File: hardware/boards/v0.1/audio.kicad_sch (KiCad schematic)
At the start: 45 parts, among them J4 SPKR_L, J5 SPKR_R, J8 LINE_OUT, J9 LINE_IN, U24 MIC, U28 TS5A23159RSE, U29 NAU88C22YG, U34 SI4710-B30-GMR, U35 SI4703-C19-GMR, Y3 ASVK-32.768KHZ-LJ-T

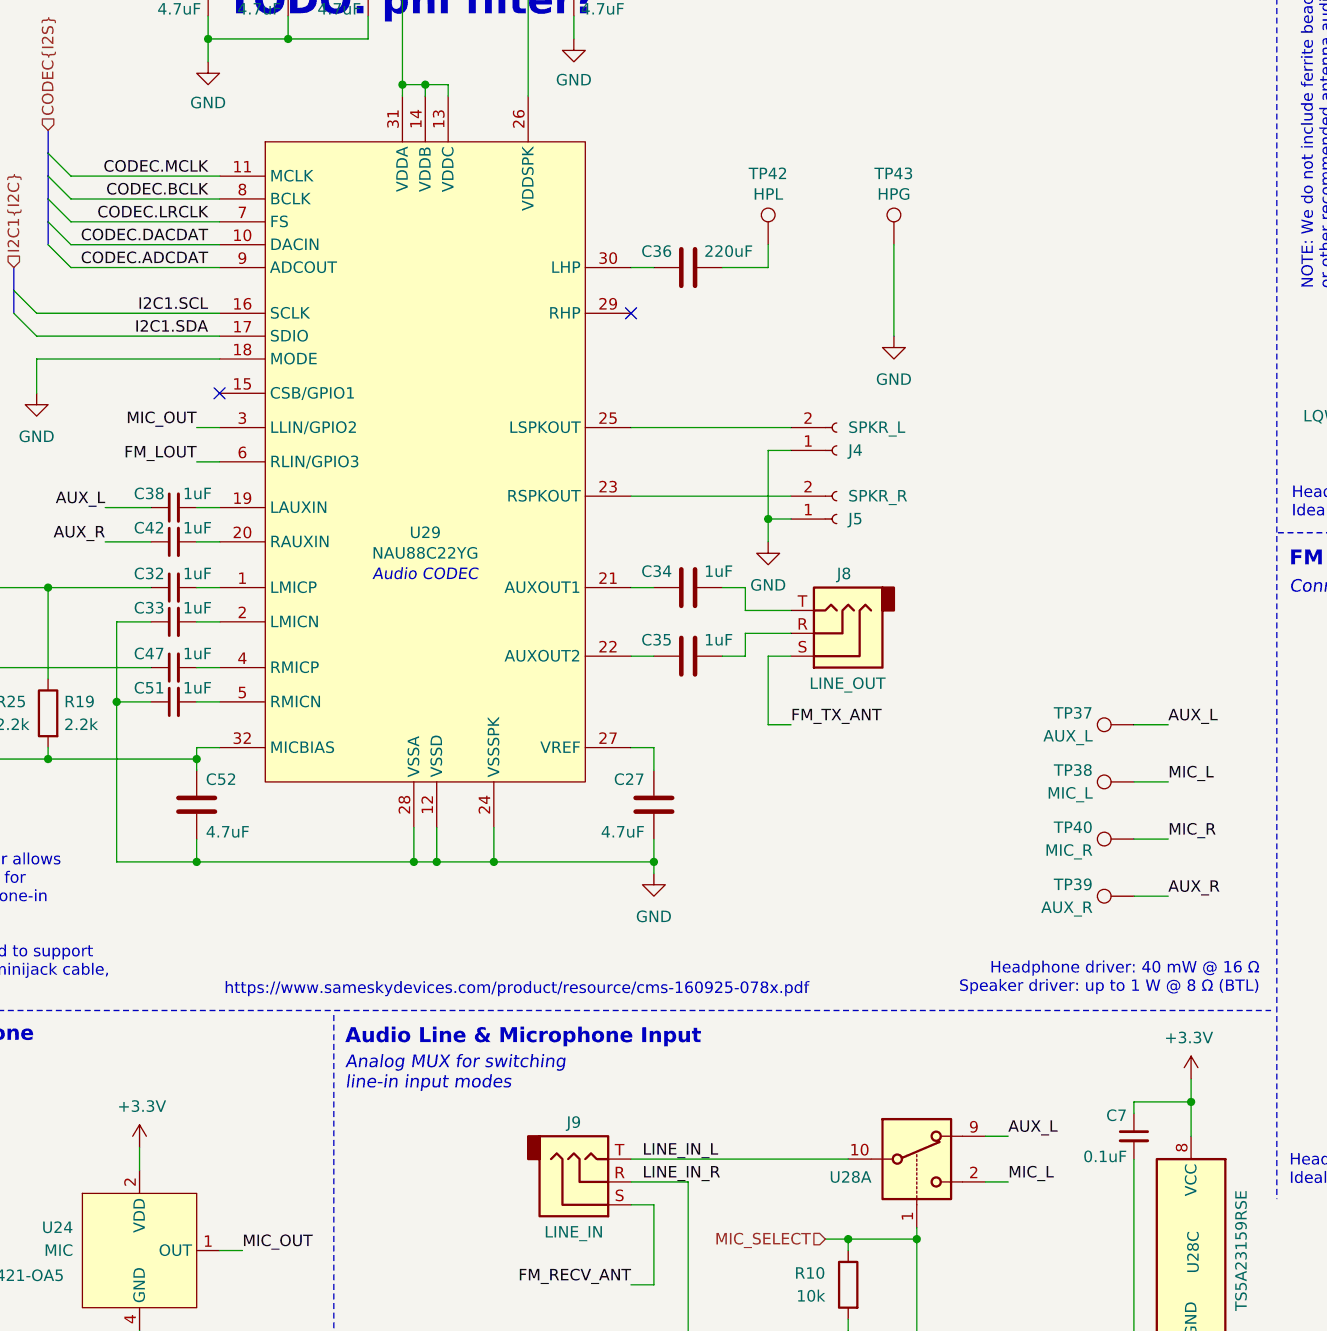
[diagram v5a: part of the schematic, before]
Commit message: feat: routing cleanup and start of BOM selection
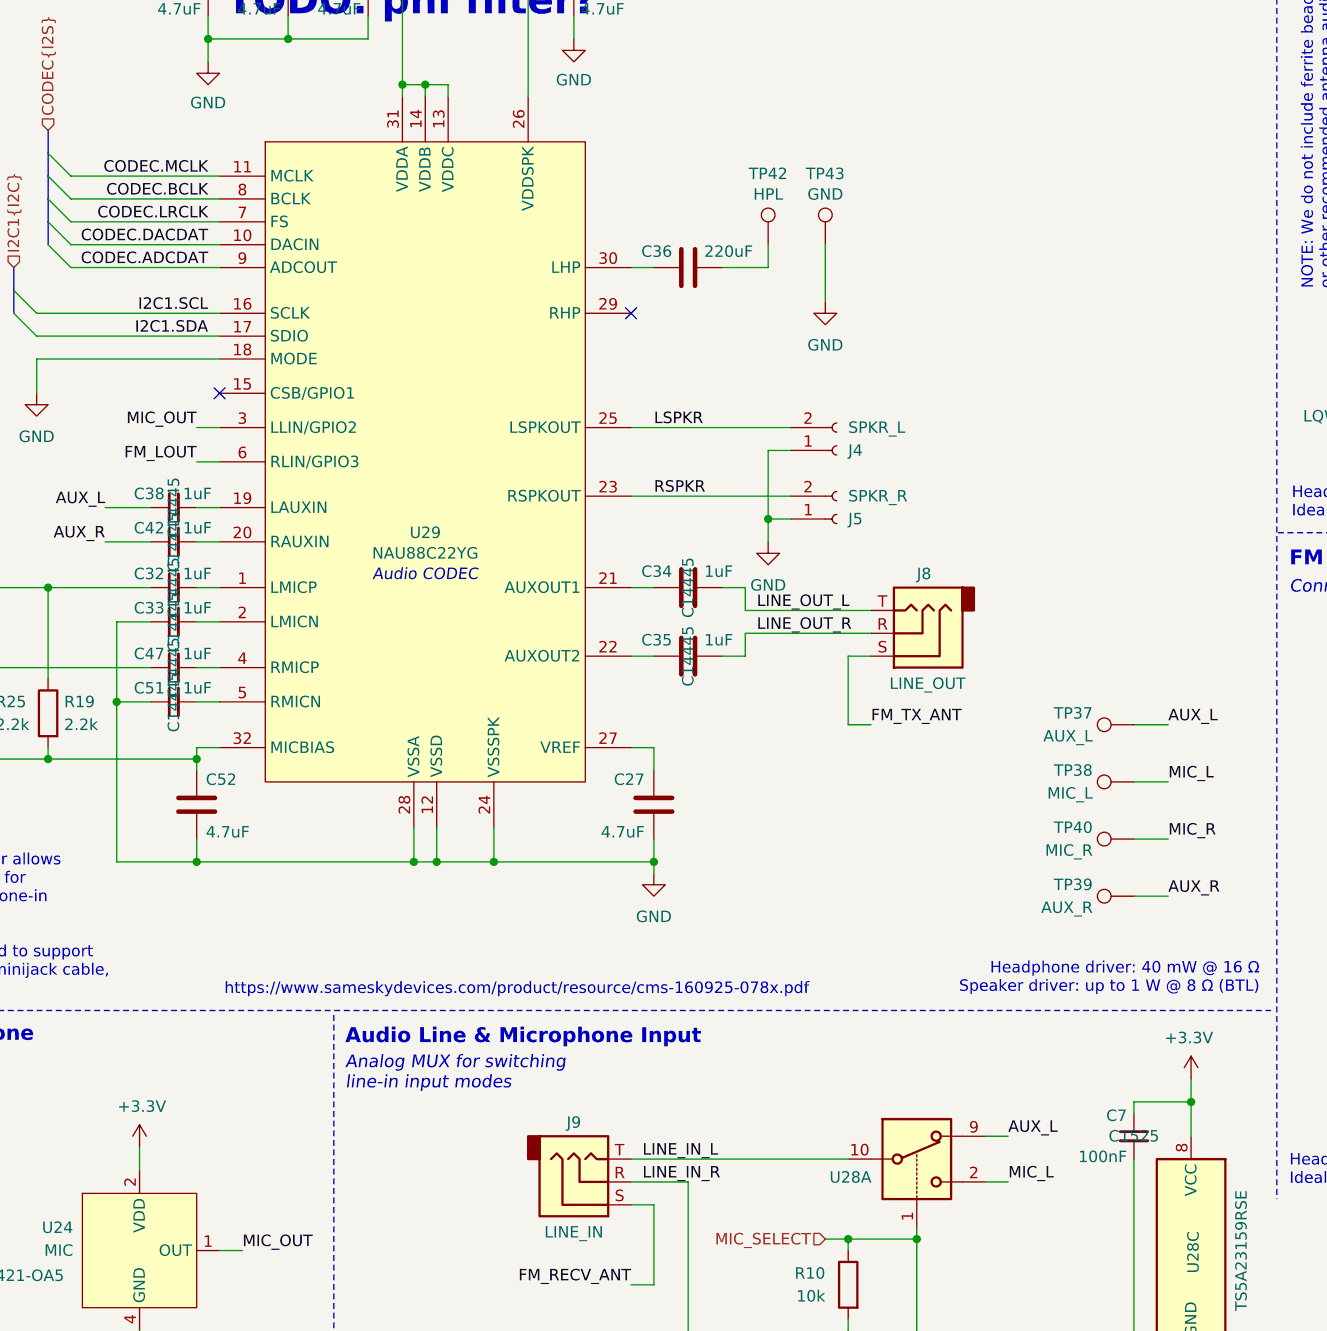
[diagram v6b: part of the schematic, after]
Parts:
- C32, C33, C34, C35, C47, C51: footprint Capacitor_SMD:C_0603_1608Metric -> Capacitor_SMD:C_0402_1005Metric; JLC (none) -> C14445
- C36: footprint Capacitor_SMD:C_0603_1608Metric -> Capacitor_SMD:C_0402_1005Metric
- C38, C42: JLC (none) -> C14445
- C7: value 0.1uF -> 100nF; footprint Capacitor_SMD:C_0603_1608Metric -> Capacitor_SMD:C_0402_1005Metric; JLC (none) -> C1525
- J8, J9: JLC C4991872 -> (none)
- R10: footprint Resistor_SMD:R_0603_1608Metric -> Resistor_SMD:R_0402_1005Metric; JLC (none) -> C25531
- TP35, TP36, TP37, TP38, TP39, TP40, TP42: now left out of the parts list
- TP43: value HPG -> GND; now left out of the parts list
- U35: JLC (none) -> C2155582
- Y3: JLC (none) -> C17591433
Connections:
- net LINE_OUT_R: now reaches C35.2, J8.R
- net LINE_OUT_L: now reaches C34.2, J8.T
- net RSPKR: now reaches J5.2 (Pin_2), U29.23 (RSPKOUT)
- net LSPKR: now reaches J4.2 (Pin_2), U29.25 (LSPKOUT)
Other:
- moved on the sheet: J8

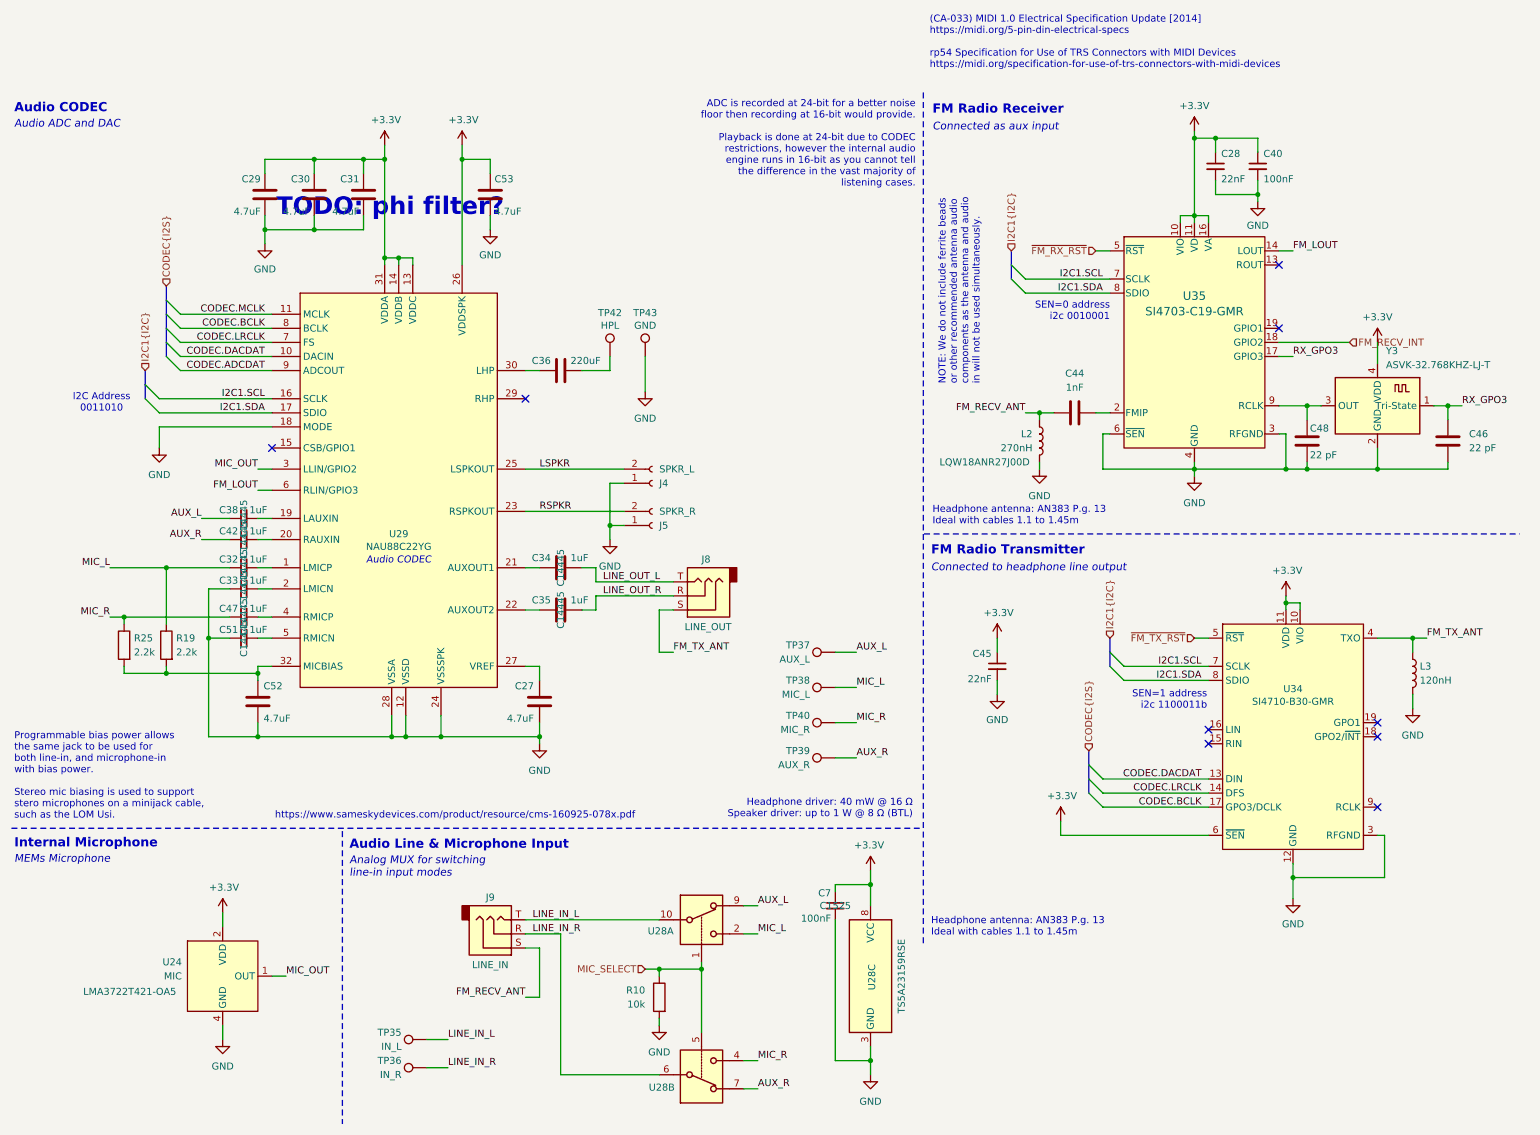
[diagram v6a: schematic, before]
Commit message: feat: update various components to 0402
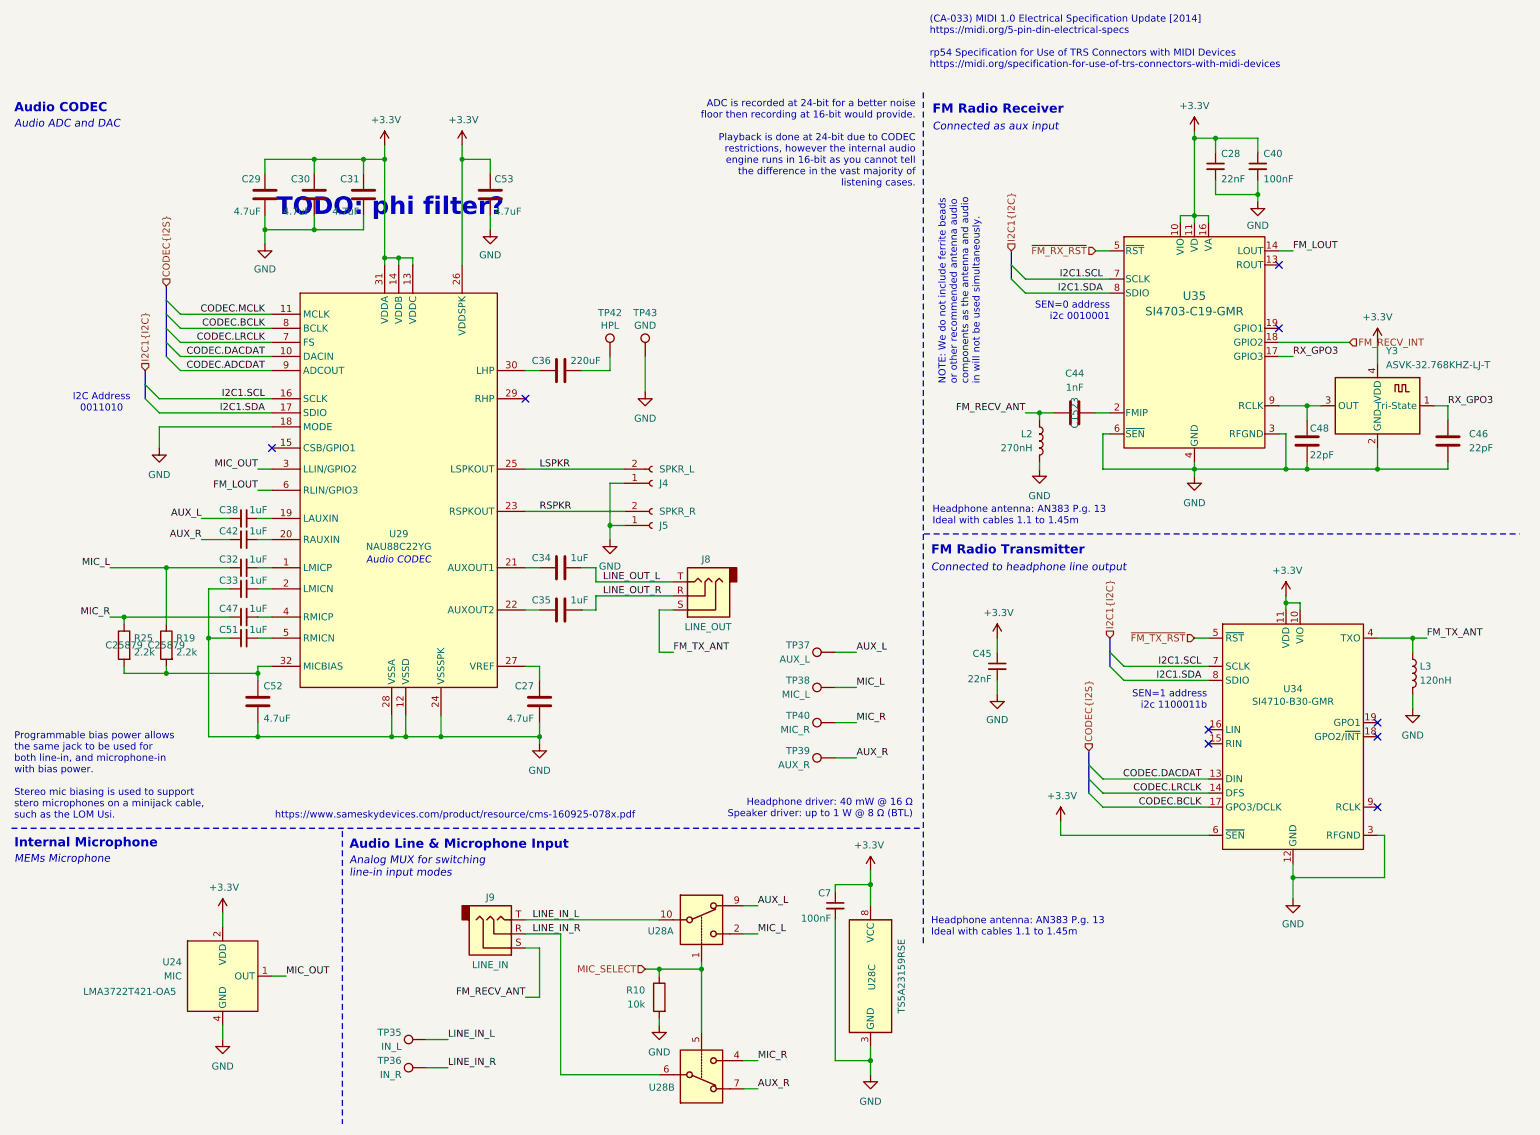
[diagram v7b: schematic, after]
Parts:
- C27, C29, C30, C31, C52, C53: footprint Capacitor_SMD:C_0603_1608Metric -> Capacitor_SMD:C_0402_1005Metric; JLC (none) -> C23733
- C28, C45: footprint Capacitor_SMD:C_0603_1608Metric -> Capacitor_SMD:C_0402_1005Metric; JLC (none) -> C1532
- C40: footprint Capacitor_SMD:C_0603_1608Metric -> Capacitor_SMD:C_0402_1005Metric; JLC (none) -> C1525
- C44: footprint Capacitor_SMD:C_0603_1608Metric -> Capacitor_SMD:C_0402_1005Metric; JLC (none) -> C1523
- C46, C48: value 22 pF -> 22pF; footprint Capacitor_SMD:C_0603_1608Metric -> Capacitor_SMD:C_0402_1005Metric; JLC (none) -> C1555
- L2: Part LQW18ANR27J00D -> (none)
- R19, R25: footprint Resistor_SMD:R_0603_1608Metric -> Resistor_SMD:R_0402_1005Metric; JLC (none) -> C25879

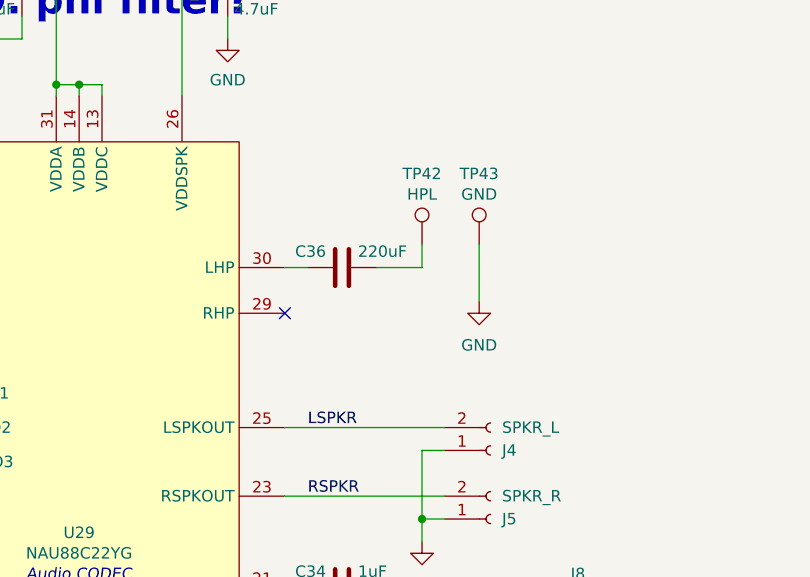
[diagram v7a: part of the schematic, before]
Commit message: feat: various DFM cleanup steps
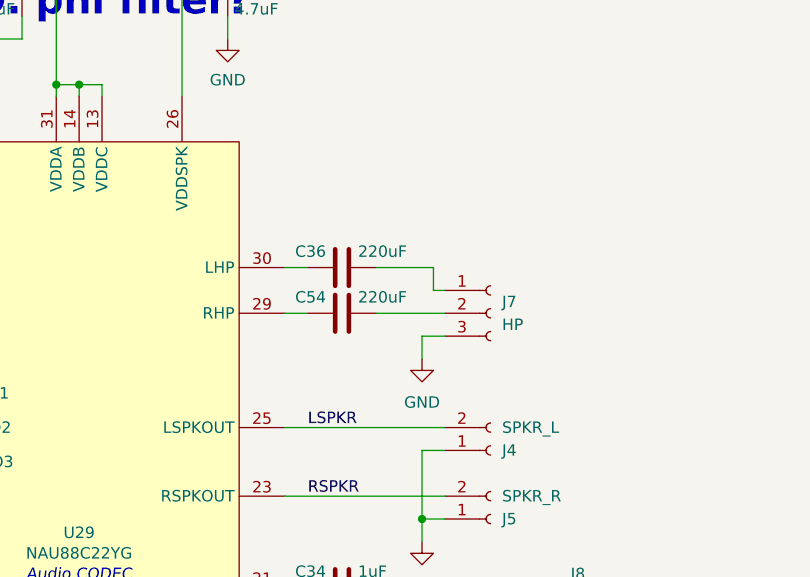
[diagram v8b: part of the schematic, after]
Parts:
- removed TP42: HPL, TestPoint:TestPoint_Pad_D2.0mm, symbol Connector:TestPoint
- removed TP43: GND, TestPoint:TestPoint_Pad_D2.0mm, symbol Connector:TestPoint
- added C54: 220uF, Capacitor_SMD:C_0402_1005Metric, symbol Device:C
- added J7: HP, Connector_PinHeader_2.00mm:PinHeader_1x03_P2.00mm_Vertical, symbol Connector:Conn_01x03_Socket
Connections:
- net EPAD: now also J7.3 (Pin_3)
- net at U29.29 (RHP): now also C54.1
- net at C36.2: now also J7.1 (Pin_1)
- new net: C54.2, J7.2 (Pin_2)
- no-connect marks 9 -> 8
